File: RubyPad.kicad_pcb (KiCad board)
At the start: 2 copper layers, 72 x 42 mm, 24 parts, among them J1 USB_mini_micro_B, K1 KEYSW, K2 KEYSW, K3 KEYSW, K4 KEYSW, SW1 SW_PUSH, U1 ATMEGA32U4, X1 XTAL_GND

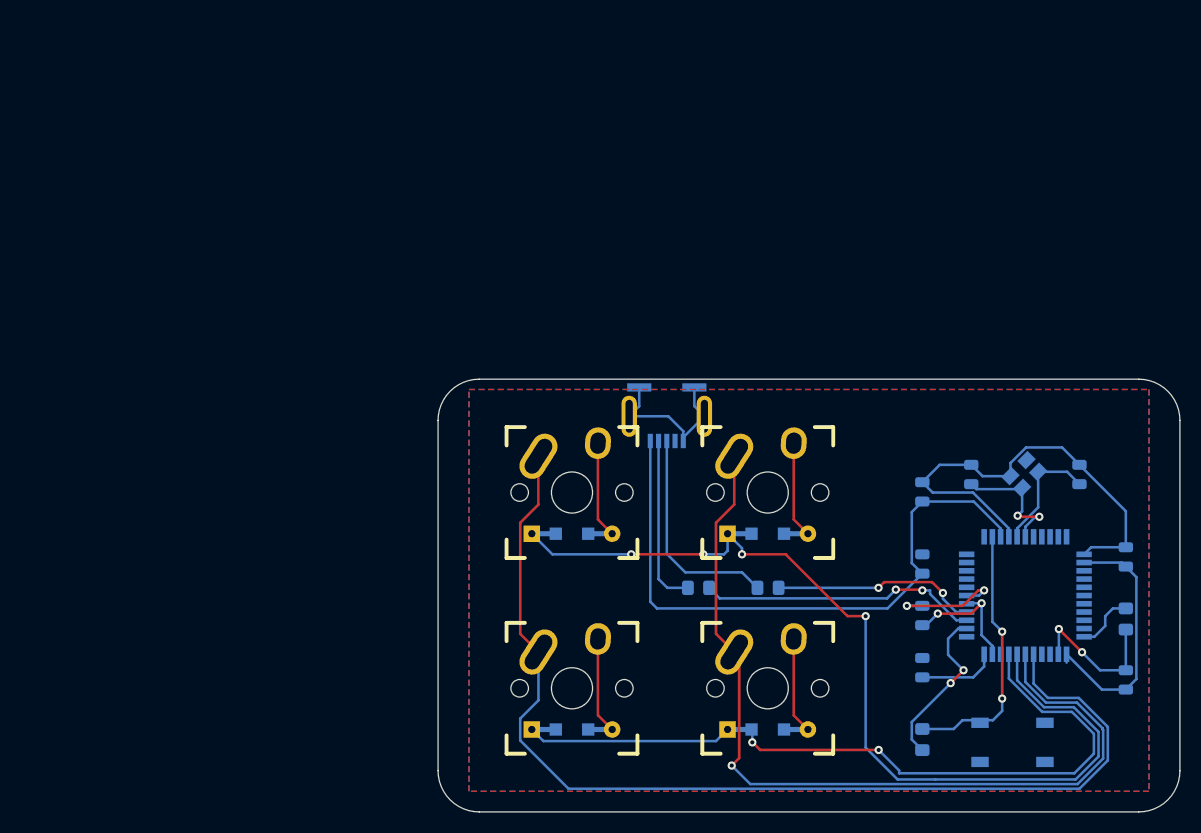
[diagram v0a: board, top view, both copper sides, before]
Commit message: Redone the pcb again but forgot the 'fill area' thing
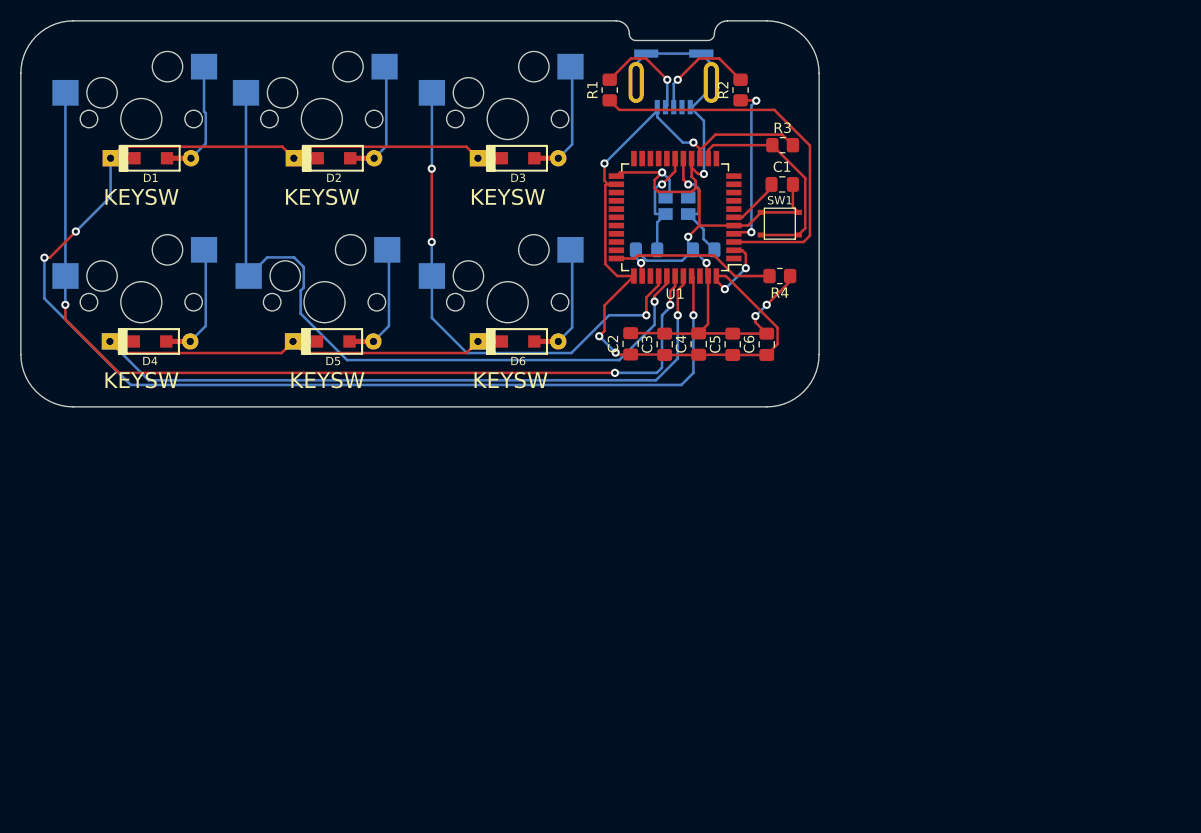
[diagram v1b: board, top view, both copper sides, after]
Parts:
- added D5: D, keyboard_parts:D_SOD123_axial, F.Cu at (46.8, 53.3)
- added D6: D, keyboard_parts:D_SOD123_axial, F.Cu at (64.8, 53.3)
- added G***: LOGO, ruby:logo_small, B.Cu at (74.9, 45.7)
- added K5: KEYSW, HotSwap:Kailh_MX_Socket, B.Cu at (46.0, 49.5)
- added K6: KEYSW, HotSwap:Kailh_MX_Socket, B.Cu at (63.8, 49.5)
- C1: value 0.1u -> 1u; footprint Capacitor_SMD:C_0805_2012Metric -> Capacitor_SMD:C_0805_2012Metric_Pad1.18x1.45mm_HandSolder; moved to F.Cu
- C2, C3, C4: footprint Capacitor_SMD:C_0805_2012Metric -> Capacitor_SMD:C_0805_2012Metric_Pad1.18x1.45mm_HandSolder; moved to F.Cu
- C5: value 4.7u -> 0.1u; footprint Capacitor_SMD:C_0805_2012Metric -> Capacitor_SMD:C_0805_2012Metric_Pad1.18x1.45mm_HandSolder; moved to F.Cu
- C6: value 22p -> 4.7u; footprint Capacitor_SMD:C_0805_2012Metric -> Capacitor_SMD:C_0805_2012Metric_Pad1.18x1.45mm_HandSolder; moved to F.Cu
- C7: footprint Capacitor_SMD:C_0805_2012Metric -> Capacitor_SMD:C_0805_2012Metric_Pad1.18x1.45mm_HandSolder
- C8: value 1u -> 22p; footprint Capacitor_SMD:C_0805_2012Metric -> Capacitor_SMD:C_0805_2012Metric_Pad1.18x1.45mm_HandSolder
- D1, D2, D3, D4, U1: moved to F.Cu
- K1, K2, K3, K4: footprint keebs:Mx_Alps_100 -> HotSwap:Kailh_MX_Socket; moved to B.Cu
- R1: value 10k -> 22; footprint Resistor_SMD:R_0805_2012Metric_Pad1.15x1.40mm_HandSolder -> Resistor_SMD:R_0805_2012Metric_Pad1.20x1.40mm_HandSolder; moved to F.Cu
- R2, R4: footprint Resistor_SMD:R_0805_2012Metric_Pad1.15x1.40mm_HandSolder -> Resistor_SMD:R_0805_2012Metric_Pad1.20x1.40mm_HandSolder; moved to F.Cu
- R3: value 22 -> 10k; footprint Resistor_SMD:R_0805_2012Metric_Pad1.15x1.40mm_HandSolder -> Resistor_SMD:R_0805_2012Metric_Pad1.20x1.40mm_HandSolder; moved to F.Cu
- SW1: footprint Button_Switch_SMD:SW_SPST_TL3342 -> Keebio-Parts:SW_SPST_3x3; moved to F.Cu
- moved K1 82.2 mm to (28.2, 31.8), turned to 180 degrees
- moved D1 81.6 mm to (29.1, 35.6)
- moved R1 70.0 mm to (73.7, 28.9), turned to 90 degrees
- moved K2 56.5 mm to (45.7, 31.8), turned to 180 degrees
- moved D3 55.7 mm to (64.8, 35.6)
- moved D2 55.7 mm to (46.9, 35.6)
- moved K3 55.6 mm to (63.8, 31.8), turned to 180 degrees
- moved SW1 55.2 mm to (90.2, 41.9)
- moved C4 52.7 mm to (82.3, 53.6)
- moved C2 52.3 mm to (75.7, 53.6)
- moved U1 50.0 mm to (80.0, 41.3), turned to 180 degrees
- moved R2 48.5 mm to (86.4, 28.9), turned to 90 degrees
- moved R4 47.3 mm to (90.2, 47.0), turned to 180 degrees
- moved K4 45.7 mm to (28.2, 49.5), turned to 180 degrees
- moved D4 45.0 mm to (29.1, 53.3)
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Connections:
- C1 pad 1: VCC -> Net-(C1-Pad1)
- C6 pad 1: Net-(C6-Pad1) -> VCC
- D2 pad 1: /row1 -> /row0
- K2 pad 1: /col0 -> /col1
- K3 pad 1: /col1 -> /col2
- K4 pad 1: /col1 -> /col0
- R1 pad 2: VCC -> Net-(J1-Pad2)
- R2 pad 2: Net-(J1-Pad2) -> Net-(J1-Pad3)
- R3 pad 2: Net-(J1-Pad3) -> VCC
- SW1 pad 2: Net-(R1-Pad1) -> Net-(R3-Pad1)
- U1 pad 13: Net-(R1-Pad1) -> Net-(R3-Pad1)
- U1 pad 16: Net-(C6-Pad1) -> Net-(C7-Pad1)
- U1 pad 17: Net-(C7-Pad1) -> Net-(C8-Pad1)
- U1 pad 3: Net-(R2-Pad1) -> Net-(R1-Pad1)
- U1 pad 37: Net-(U1-Pad37) -> /col2
- U1 pad 4: Net-(R3-Pad1) -> Net-(R2-Pad1)
- U1 pad 6: Net-(C8-Pad1) -> Net-(C1-Pad1)
- X1 pad 1: Net-(C6-Pad1) -> Net-(C7-Pad1)
- X1 pad 2: Net-(C7-Pad1) -> Net-(C8-Pad1)
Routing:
- net /row0: track 71.3 -> 130.5 mm, vias 2 -> 4
- net /col2: track 0.00 -> 49.9 mm, vias 0 -> 3
- net /col1: track 104.9 -> 71.9 mm, vias 0 -> 1
- net VCC: track 110.6 -> 83.3 mm, vias 2 -> 6
- net /row1: track 91.1 -> 103.5 mm, vias 4 -> 1
- net Net-(R1-Pad1): track 25.8 -> 37.6 mm, vias 2 -> 0
- net Net-(C6-Pad1): track 11.7 -> 0.00 mm
- net GND: track 88.8 -> 100.1 mm, vias 4 -> 7
- net Net-(R2-Pad1): track 27.2 -> 16.3 mm
- net Net-(J1-Pad3): track 21.1 -> 10.6 mm, vias 0 -> 1
- net Net-(R4-Pad2): track 5.75 -> 15.8 mm
- net Net-(D5-Pad2): track 0.00 -> 9.58 mm
- net Net-(D6-Pad2): track 0.00 -> 9.52 mm
- net /col0: track 84.8 -> 91.7 mm, vias 1 -> 3
- net Net-(J1-Pad2): track 16.6 -> 10.0 mm, vias 0 -> 1
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- removed copper zone on F.Cu, net (none)
- removed copper zone on B.Cu, net GND
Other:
- board size 72 x 42 mm -> 77.5 x 37.5 mm
